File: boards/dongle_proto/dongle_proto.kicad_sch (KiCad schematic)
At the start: 40 parts, among them J1 Conn_ARM_JTAG_SWD_10, J2 Screw_Terminal_01x02, J3 Screw_Terminal_01x04, Q1 MMBT4403, SW1 2223-TS02-66-70-BK-160-LCR-D-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, SW2 2223-TS02-66-70-BK-160-LCR-D-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, U1 HX711, U2 pca10059

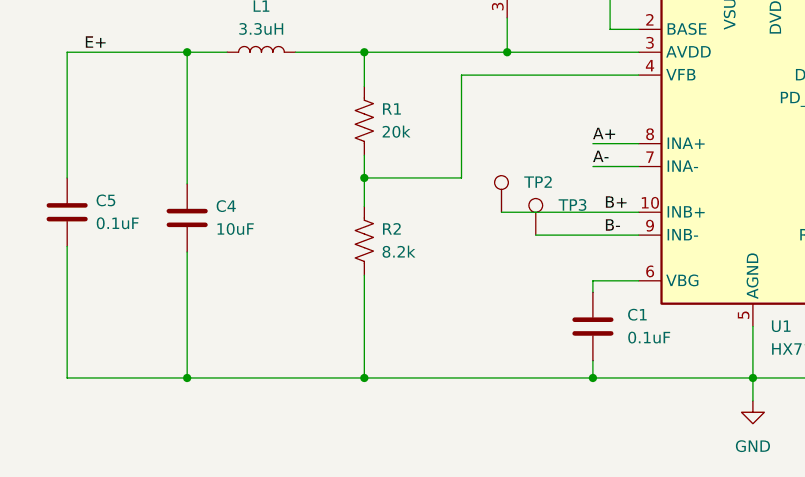
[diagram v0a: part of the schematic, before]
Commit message: Fix HX711 AVDD level
The HX711's analog output (AVDD) should be set below its supply voltage
(the battery voltage) so that the chip's feedback loop can create a
stable excitation voltage that is resilient to load transients. The
R1/R2 resistor ladder was set such that AVDD would always rail to the
supply voltage. Set it to ~2.7-2.8V instead.

Note: it's possible that this doesn't actually matter since the ADC
makes ratiometric measurements (the reference is the same as the supply
voltage) and may actually hurt SNR.
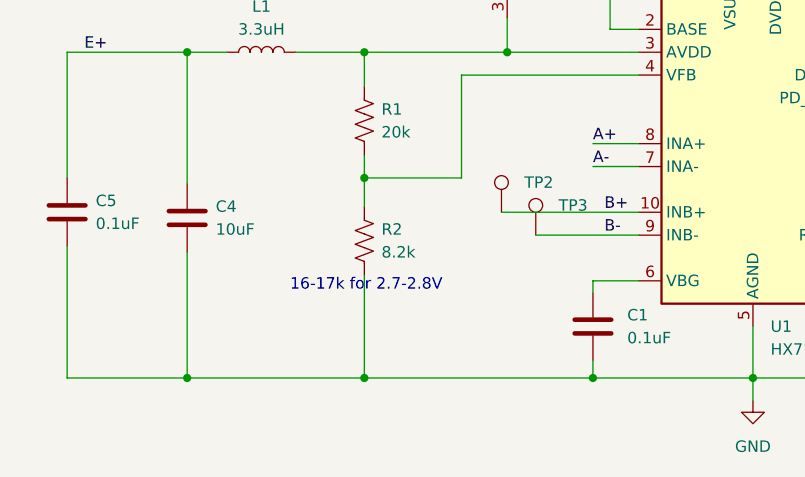
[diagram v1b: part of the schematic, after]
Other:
- note added: "16-17k for 2.7-2.8V"
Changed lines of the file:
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@@
+    (effects (font (size 1.27 1.27)) (justify left bottom))
+  )
+  (text "16-17k for 2.7-2.8V" (at 49.53 175.26 0)
     (effects (font (size 1.27 1.27)) (justify left bottom))
   )
